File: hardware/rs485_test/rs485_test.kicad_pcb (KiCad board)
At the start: 2 copper layers, 25 parts, among them J1 CNC Tech 3020-10-0100-00‎, J10 Conn_01x02_Male, J2 Conn_01x02_Male, J3 CNC Tech 3020-10-0100-00‎, J4 Conn_01x02_Male, J5 CNC Tech 3020-10-0100-00‎, J6 Conn_01x02_Male, J7 CNC Tech 3020-10-0100-00‎, J8 Conn_01x02_Male, J9 CNC Tech 3020-10-0100-00‎, U1 24LC024-I/SN, U2 24LC024-I/SN, U3 24LC024-I/SN, U4 24LC024-I/SN, U5 24LC024-I/SN

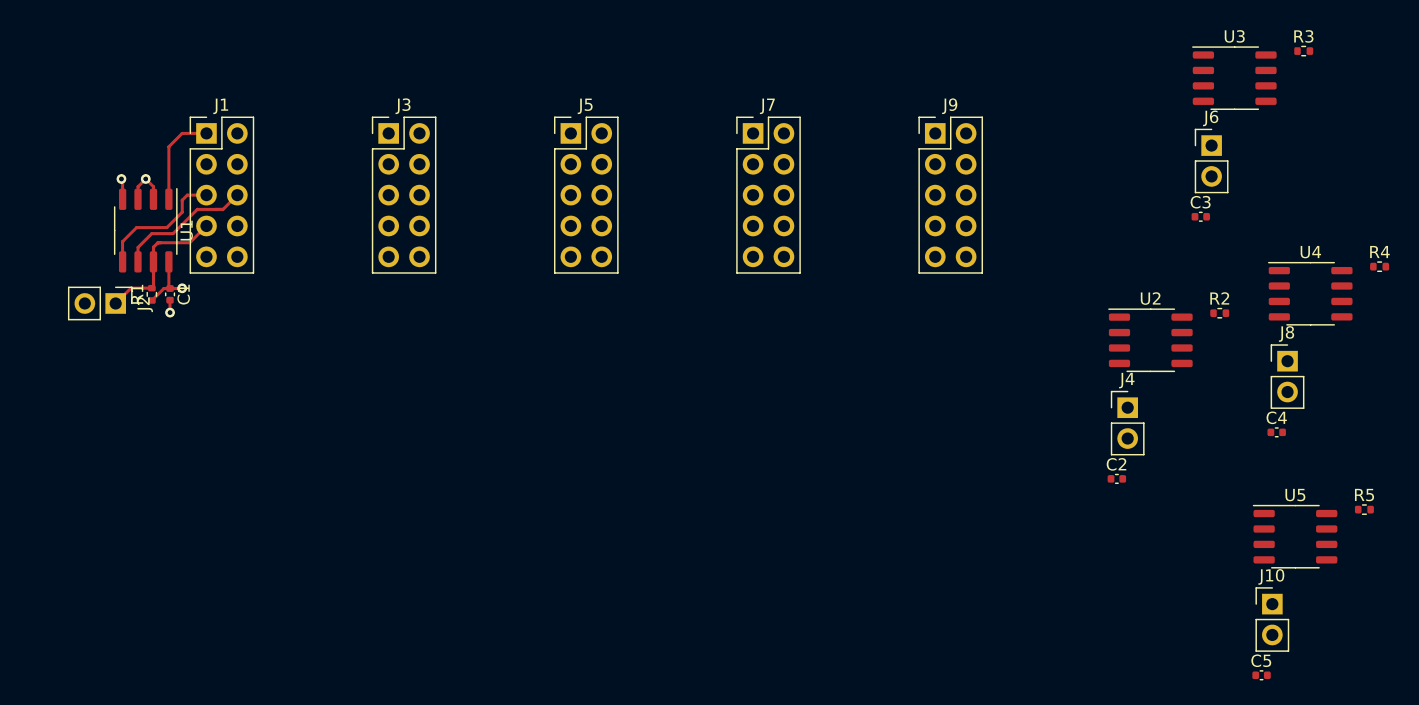
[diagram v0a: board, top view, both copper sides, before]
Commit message: Added RS485 driver and AXI GPIO for read/write
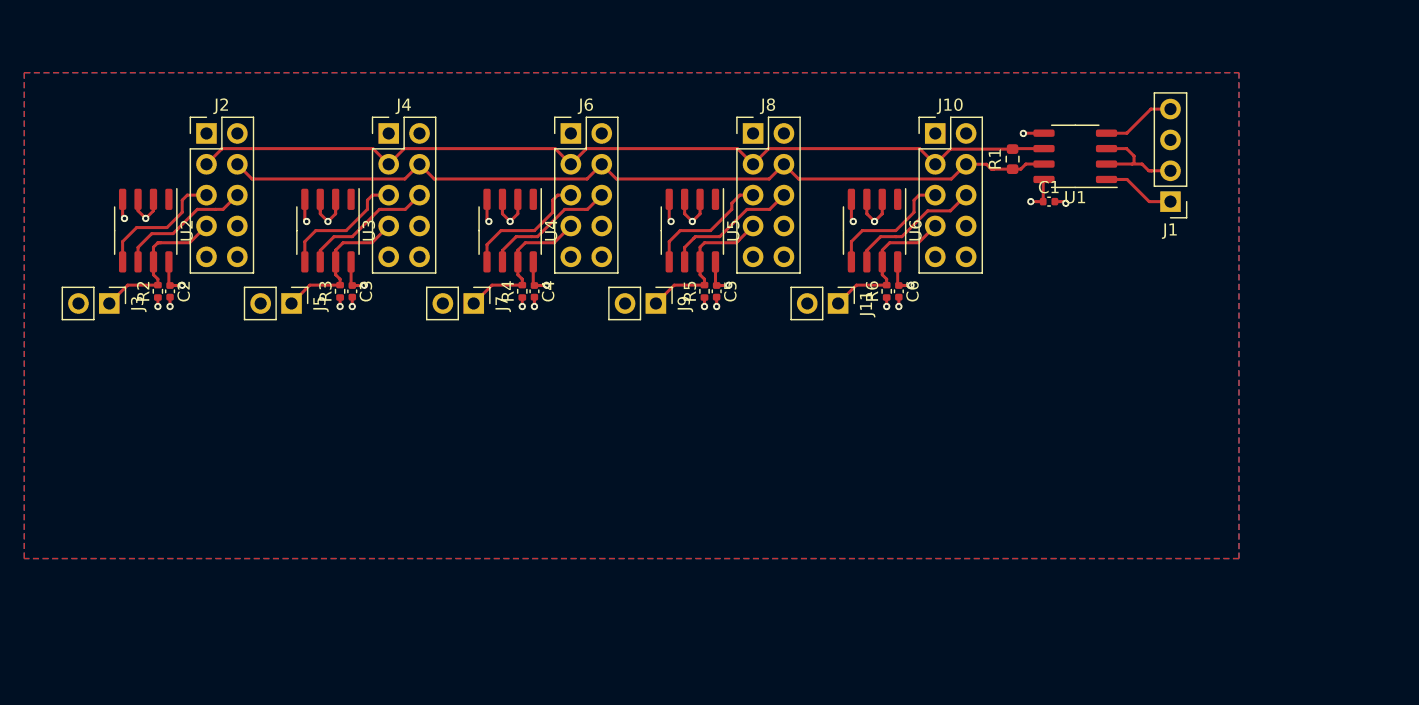
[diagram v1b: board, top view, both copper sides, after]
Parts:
- added C1: 100n, Capacitor_SMD:C_0402_1005Metric, F.Cu at (169.4, 105.6)
- added J1: Conn_01x04_Male, Connector_PinHeader_2.54mm:PinHeader_1x04_P2.54mm_Vertical, F.Cu at (179.4, 105.6)
- added R1: 120, Resistor_SMD:R_0603_1608Metric, F.Cu at (166.4, 102.1)
- added U1: MAX3483ESA+, Package_SO:SO-8_3.9x4.9mm_P1.27mm, F.Cu at (171.5, 101.9)
- moved R3 72.4 mm to (111.0, 113.0), turned to 90 degrees
- moved J5 69.4 mm to (107.0, 114.0), turned to -90 degrees
- moved U3 68.3 mm to (110.0, 108.0), turned to -90 degrees
- moved R4 67.3 mm to (126.0, 113.0), turned to 90 degrees
- moved C3 64.8 mm to (112.0, 113.0), turned to -90 degrees
- moved J7 62.1 mm to (122.0, 114.0), turned to -90 degrees
- moved U4 61.0 mm to (125.0, 108.0), turned to -90 degrees
- moved R5 55.6 mm to (141.0, 113.0), turned to 90 degrees
- moved C4 55.2 mm to (127.0, 113.0), turned to -90 degrees
- moved J9 52.2 mm to (137.0, 114.0), turned to -90 degrees
- moved U5 51.2 mm to (140.0, 108.0), turned to -90 degrees
- moved C5 47.5 mm to (142.0, 113.0), turned to -90 degrees
- moved C6 43.5 mm to (157.0, 113.0), turned to -90 degrees
- moved J11 43.5 mm to (152.0, 114.0), turned to -90 degrees
- moved R6 43.2 mm to (156.0, 113.0), turned to 90 degrees
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- renumbered C1 to C2, C2 to C3, C3 to C4, C4 to C5, C5 to C6, J9 to J10, J10 to J11, J1 to J2, J2 to J3, J3 to J4, J4 to J5, J5 to J6, J6 to J7, J7 to J8, J8 to J9, R1 to R2, R2 to R3, R3 to R4, R4 to R5, R5 to R6, U1 to U2, U2 to U3, U3 to U4, U4 to U5, U5 to U6
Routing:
- net RS485_A: track 0.00 -> 73.8 mm
- net RS485_B: track 0.00 -> 70.9 mm
- net GND: track 6.91 -> 38.0 mm, vias 3 -> 17
- net Net-(J8-Pad7): track 0.00 -> 13.3 mm
- net Net-(J10-Pad7): track 0.00 -> 12.8 mm
- net Net-(J6-Pad7): track 0.00 -> 12.8 mm
- net Net-(J4-Pad7): track 0.00 -> 12.8 mm
- net Net-(J8-Pad6): track 0.00 -> 11.1 mm
- net Net-(J6-Pad6): track 0.00 -> 11.0 mm
- net Net-(J4-Pad6): track 0.00 -> 11.0 mm
- net Net-(J10-Pad6): track 0.00 -> 11.0 mm
- net Net-(J10-Pad5): track 0.00 -> 10.7 mm
- net Net-(J6-Pad5): track 0.00 -> 10.6 mm
- net Net-(J4-Pad5): track 0.00 -> 10.6 mm
- net Net-(J8-Pad5): track 0.00 -> 10.5 mm
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- added copper zone on B.Cu, net GND
- added copper zone on F.Cu, net GND

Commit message: Added RS485 test board
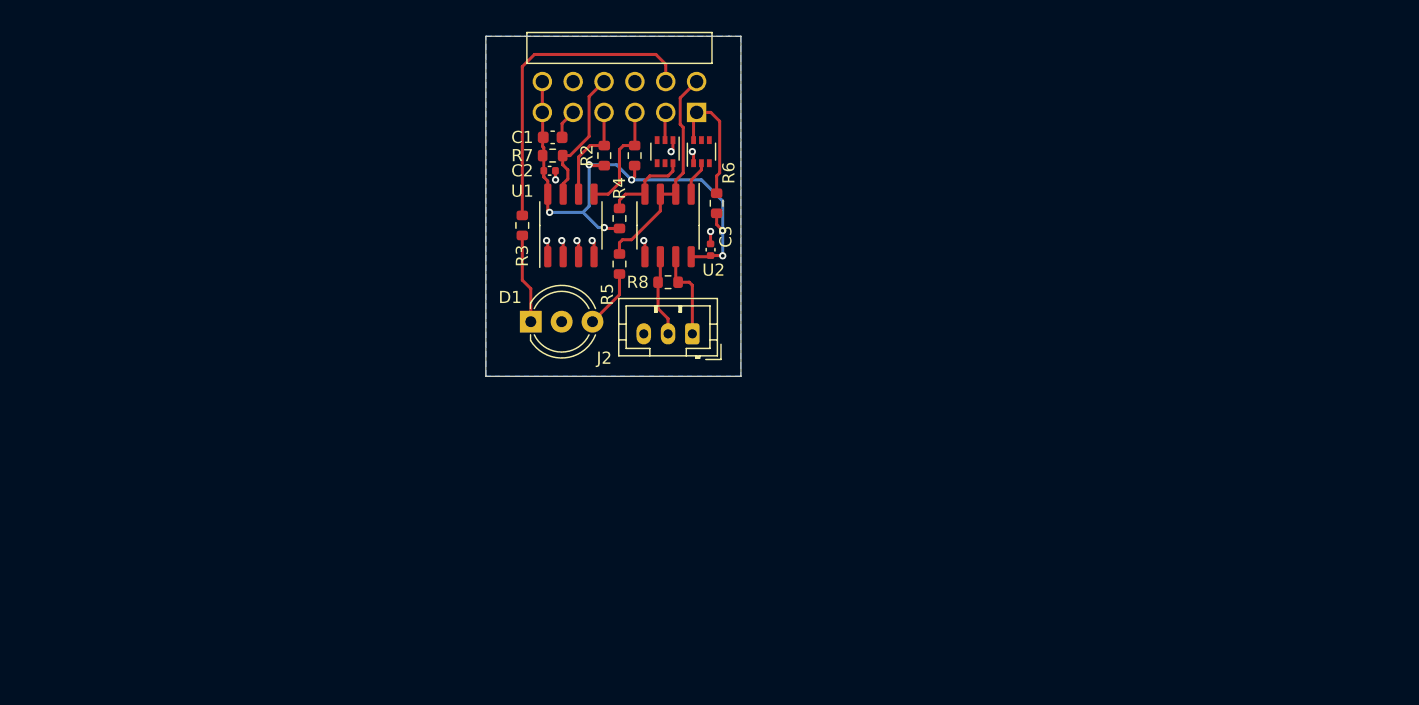
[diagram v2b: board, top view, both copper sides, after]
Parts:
- removed C4, C5, C6: 100n, Capacitor_SMD:C_0402_1005Metric
- removed J10, J4, J6, J8: CNC Tech 3020-10-0100-00‎, Connector_PinHeader_2.54mm:PinHeader_2x05_P2.54mm_Vertical
- removed J11, J3, J5, J7, J9: Conn_01x02_Male, Connector_PinHeader_2.54mm:PinHeader_1x02_P2.54mm_Vertical
- removed U3, U4, U5, U6: 24LC024-I/SN, Package_SO:SO-8_3.9x4.9mm_P1.27mm
- added D1: LED_Dual_AKA, LED_THT:LED_D5.0mm-3, F.Cu at (126.7, 115.5)
- added Q1: SI1539CDL-T1-GE3, Package_TO_SOT_SMD:SOT-363_SC-70-6, F.Cu at (137.8, 101.5)
- added Q2: SI1539CDL-T1-GE3, Package_TO_SOT_SMD:SOT-363_SC-70-6, F.Cu at (140.8, 101.5)
- added R7: 1k, Resistor_SMD:R_0603_1608Metric, F.Cu at (128.5, 101.8)
- added R8: 120, Resistor_SMD:R_0603_1608Metric, F.Cu at (138.0, 112.2)
- C1: value 100n -> 10u; footprint Capacitor_SMD:C_0402_1005Metric -> Capacitor_SMD:C_0603_1608Metric
- J1: value Conn_01x04_Male -> Connector_PMOD_2x6_Peripheral; footprint Connector_PinHeader_2.54mm:PinHeader_1x04_P2.54mm_Vertical -> Connector_WUT:PMOD_Wurth_61301221021_Horizontal
- J2: value CNC Tech 3020-10-0100-00‎ -> Conn_01x03_Male; footprint Connector_PinHeader_2.54mm:PinHeader_2x05_P2.54mm_Vertical -> Connector_JST:JST_PH_B3B-PH-K_1x03_P2.00mm_Vertical
- R1: value 120 -> 4k7
- R2: value 1k -> 4k7; footprint Resistor_SMD:R_0402_1005Metric -> Resistor_SMD:R_0603_1608Metric
- R3, R5, R6: value 1k -> R; footprint Resistor_SMD:R_0402_1005Metric -> Resistor_SMD:R_0603_1608Metric
- R4: value 1k -> 10k; footprint Resistor_SMD:R_0402_1005Metric -> Resistor_SMD:R_0603_1608Metric
- U1: value MAX3483ESA+ -> 24LC024-I/SN
- U2: value 24LC024-I/SN -> MAX3483ESA+
- moved J1 46.2 mm to (134.0, 97.0), turned to 0 degrees
- moved J2 43.3 mm to (140.0, 116.5), turned to 180 degrees
- moved U2 43.0 mm to (138.0, 107.6)
- moved U1 41.9 mm to (130.0, 107.6), turned to 90 degrees
- moved C1 41.2 mm to (128.5, 100.3)
- moved R2 38.4 mm to (132.8, 101.8)
- moved C2 32.8 mm to (128.2, 103.1), turned to 0 degrees
- moved R1 31.1 mm to (135.2, 101.8)
- moved C3 29.7 mm to (141.5, 109.6), turned to 90 degrees
- moved R3 16.0 mm to (126.0, 107.6), turned to -90 degrees
- moved R6 15.8 mm to (142.0, 105.8)
- moved R4 10.0 mm to (134.0, 107.0)
- moved R5 7.35 mm to (134.0, 110.8), turned to -90 degrees
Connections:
- J1 pad 3: GND -> /SDA
- J1 pad 4: Net-(J1-Pad4) -> /SCL
- J2 pad 1: +3V3 -> Net-(J2-Pad1)
- J2 pad 2: GND -> Net-(J2-Pad2)
- J2 pad 3: RS485_A -> GND
- R1 pad 1: RS485_B -> +3V3
- R1 pad 2: RS485_A -> /SDA
- R2 pad 2: Net-(J2-Pad7) -> /SCL
- R3 pad 1: +3V3 -> Net-(J1-Pad8)
- R4 pad 2: Net-(J6-Pad7) -> Net-(Q1-Pad6)
- R5 pad 1: +3V3 -> Net-(J1-Pad7)
- R6 pad 2: Net-(J10-Pad7) -> Net-(J1-Pad1)
- U1 pad 1: Net-(J1-Pad1) -> GND
- U1 pad 2: Net-(J1-Pad2) -> GND
- U1 pad 3: Net-(J1-Pad2) -> GND
- U1 pad 4: Net-(J1-Pad4) -> GND
- U1 pad 5: GND -> /SDA
- U1 pad 6: RS485_A -> /SCL
- U1 pad 7: RS485_B -> /~WP
- U2 pad 1: +3V3 -> Net-(Q2-Pad2)
- U2 pad 2: GND -> Net-(J1-Pad7)
- U2 pad 3: GND -> Net-(J1-Pad7)
- U2 pad 4: GND -> Net-(Q1-Pad6)
- U2 pad 5: Net-(J2-Pad5) -> GND
- U2 pad 6: Net-(J2-Pad6) -> Net-(J2-Pad2)
- U2 pad 7: Net-(J2-Pad7) -> Net-(J2-Pad1)
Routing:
- net RS485_A: track 73.8 -> 0.00 mm
- net RS485_B: track 70.9 -> 0.00 mm
- net Net-(J1-Pad8): track 0.00 -> 26.2 mm
- net GND: track 38.0 -> 14.1 mm, vias 17 -> 9
- net +3V3: track 21.5 -> 44.4 mm, vias 11 -> 6
- net Net-(J1-Pad7): track 0.00 -> 18.2 mm
- net Net-(J2-Pad7): track 13.2 -> 0.00 mm
- net Net-(J10-Pad7): track 12.8 -> 0.00 mm
- net Net-(J6-Pad7): track 12.8 -> 0.00 mm
- net /~WP: track 0.00 -> 11.4 mm
- net Net-(J2-Pad6): track 11.2 -> 0.00 mm
- net Net-(J8-Pad6): track 11.1 -> 0.00 mm
- net Net-(J6-Pad6): track 11.0 -> 0.00 mm
- net Net-(J4-Pad6): track 11.0 -> 0.00 mm
- net Net-(J10-Pad6): track 11.0 -> 0.00 mm
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- removed copper zone on F.Cu, net GND
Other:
- board outline added: 21 x 28 mm
